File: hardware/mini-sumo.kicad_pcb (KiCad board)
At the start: 2 copper layers, 70 x 66 mm, 80 parts, among them J1 IR Sensor 1, J11 BATTERY, J12 MOTOR1, J13 MOTOR2, J14 Conn_02x03_Counter_Clockwise, J2 IR Sensor 2, J3 IR Sensor 5, J4 IR Sensor 4, J5 IR LED, J6 Floor Sensor 1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

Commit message: Finalized the PCB
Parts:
- removed J14: Conn_02x03_Counter_Clockwise, Connector_PinHeader_2.54mm:PinHeader_2x03_P2.54mm_Vertical
- added G***: LOGO, janis:erica_logo, B.Cu at (120.0, 76.8)
- added J10: Conn_02x03_Odd_Even, Connector_PinHeader_2.54mm:PinHeader_2x03_P2.54mm_Vertical, F.Cu at (132.5, 54.0)
- U10, U3, U5, U6, U7, U9: footprint janis:WS2812B -> janis:WS2812B_handsolder
- VD1: footprint Diodes_THT:D_DO-35_SOD27_P2.54mm_Vertical_AnodeUp -> Diode_THT:D_DO-35_SOD27_P2.54mm_Vertical_AnodeUp
- moved C15 0.25 mm to (146.0, 61.8)
- moved C6 0.25 mm to (94.0, 64.2)
- renumbered SW2 to SW1, SW3 to SW2, SW4 to SW3, SW5 to SW4
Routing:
- net +3V3: track 184.6 -> 200.8 mm, vias 2 -> 3
- net /GPIO41: track 0.00 -> 10.3 mm
- net /GPIO38: track 0.00 -> 7.49 mm
- net /GPIO39: track 0.13 -> 6.43 mm
- net /GPIO40: track 0.16 -> 5.67 mm
- net IR_SENSOR_4: track 22.8 -> 24.4 mm
- net FLR_SENSOR_2: track 25.7 -> 25.2 mm
- net Net-(J12-Pin_1): track 25.9 -> 25.4 mm
- net GND: vias 188 -> 184

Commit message: Added GND vias
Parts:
- added G***: LOGO, janis:erica_logo, F.Cu at (120.0, 76.0)
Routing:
- net GND: track 15.2 -> 21.6 mm, vias 184 -> 369
- net +5V: track 23.7 -> 25.1 mm

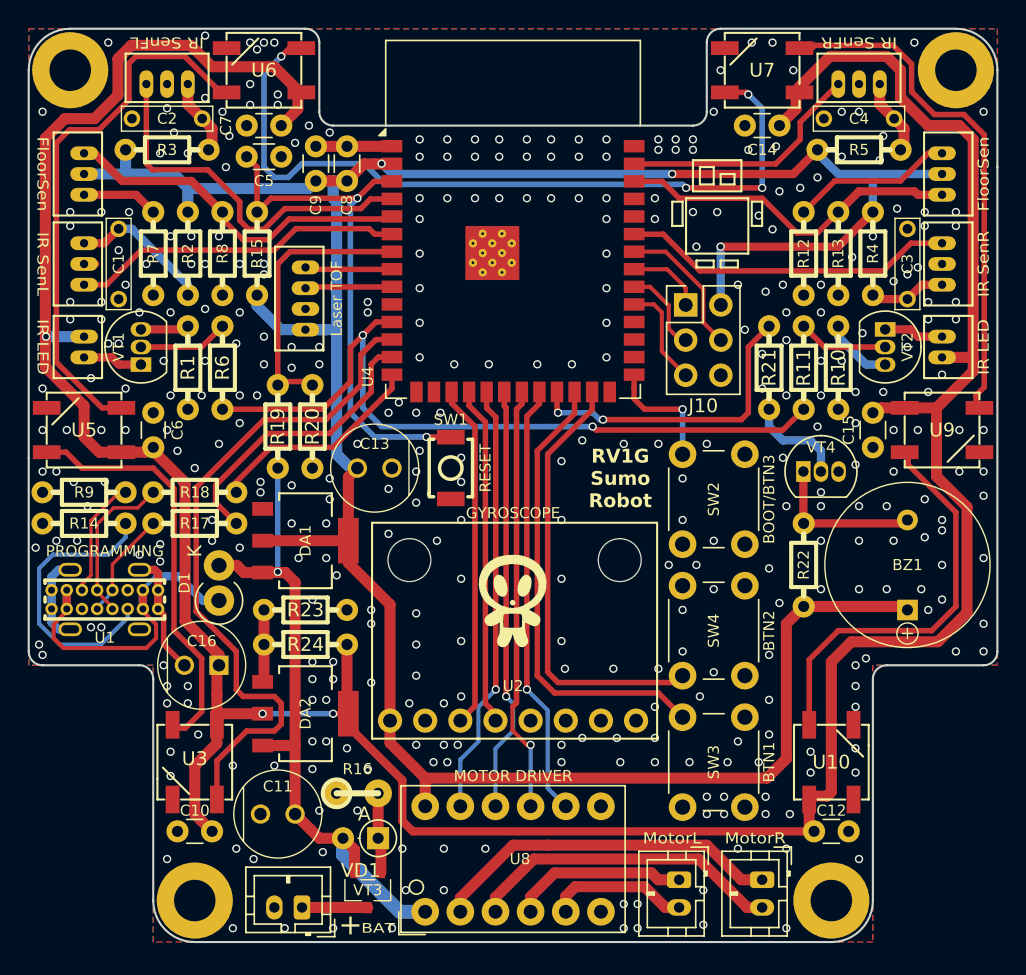
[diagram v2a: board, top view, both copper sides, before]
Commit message: Improved sikscreen on PCB. Changed reverse polarity transistor to AO3401A.
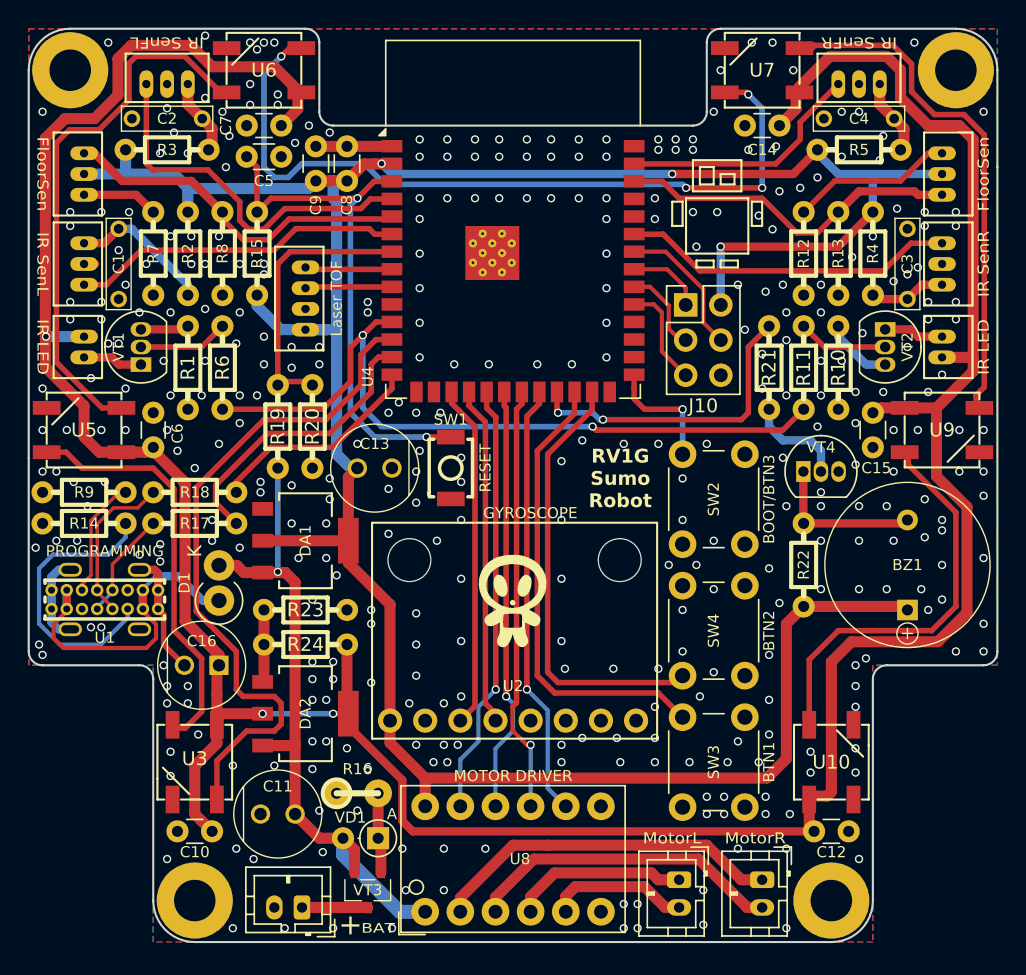
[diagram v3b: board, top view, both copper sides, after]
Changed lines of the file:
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@@
 		(tags "Diode DO-35_SOD27 series Axial Vertical pin pitch 2.54mm  length 4mm diameter 2mm")
 		(property "Reference" "VD1"
-			(at 1.27 -2.326371 180)
+			(at 2 1.5 180)
 			(layer "F.SilkS")
 			(effects
 				(font
-					(size 1 1)
+					(size 0.8 0.8)
 					(thickness 0.15)
 				)
@@
 		)
 		(fp_text user "A"
-			(at 1 1.75 180)
+			(at -1 1.75 180)
 			(layer "F.SilkS")
 			(effects
 				(font
-					(size 1 1)
+					(size 0.8 0.8)
 					(thickness 0.15)
 				)
@@
 		(tags "C Disc series Radial pin pitch 2.50mm  diameter 3.0mm width 1.6mm Capacitor")
 		(property "Reference" "C12"
-			(at 1.25 -1.5 180)
+			(at 1.25 1.5 180)
 			(layer "F.SilkS")
 			(effects
@@
 		(tags "C Disc series Radial pin pitch 2.50mm  diameter 3.0mm width 1.6mm Capacitor")
 		(property "Reference" "C10"
-			(at 1.25 1.5 180)
+			(at 1.25 -1.5 180)
 			(layer "F.SilkS")
 			(effects
@@
 		(tags "C Disc series Radial pin pitch 2.50mm  diameter 3.0mm width 1.6mm Capacitor")
 		(property "Reference" "C6"
-			(at 1.25 1.75 90)
+			(at 1 1.75 90)
 			(layer "F.SilkS")
 			(effects
@@
 		(tags "C Disc series Radial pin pitch 2.50mm  diameter 3.0mm width 1.6mm Capacitor")
 		(property "Reference" "C15"
-			(at 1.25 1.75 270)
+			(at 4 -0.25 0)
 			(layer "F.SilkS")
 			(effects
@@
 	)
 	(gr_text "GYROSCOPE"
-		(at 120 69 0)
+		(at 121.25 69 0)
 		(layer "F.SilkS")
 		(effects

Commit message: Organized and fixed schematic. Added schematic PDF and HTML interactive BOM.
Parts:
- C11, C13: value 10uF -> 100uF
- C16: value 10uF -> 47uF
- C5, C9: value 0.1uF -> 1uF
- D1: value 1N5819 -> 1N5817
- J3: value IR Sensor 5 -> IR Sensor 3
- R17, R18: value 33R -> 22R
- R20: value 10k -> 4k7
- VT3: value FDN360P -> AO3401A
